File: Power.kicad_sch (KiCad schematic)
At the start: 17 parts, among them Q1 SI2301BDS, U1 ICL7660S, X1 PEDAL_COMBO_TOP

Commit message: Initial layout
Finished the initial PCB layout.
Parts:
- removed X1: PEDAL_COMBO_TOP, Custom_Parts:PEDAL_COMBO_TOP, symbol Custom_Parts:PEDAL_COMBO_TOP
- D2: footprint Diode_SMD:D_SOD-123 -> Diode_SMD:D_SOD-323
- renumbered C4 to C3, C3 to C4, C7 to C6, C6 to C7
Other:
- moved on the sheet: C3, C5, C6, D1, D2, FB1, Q1, R2

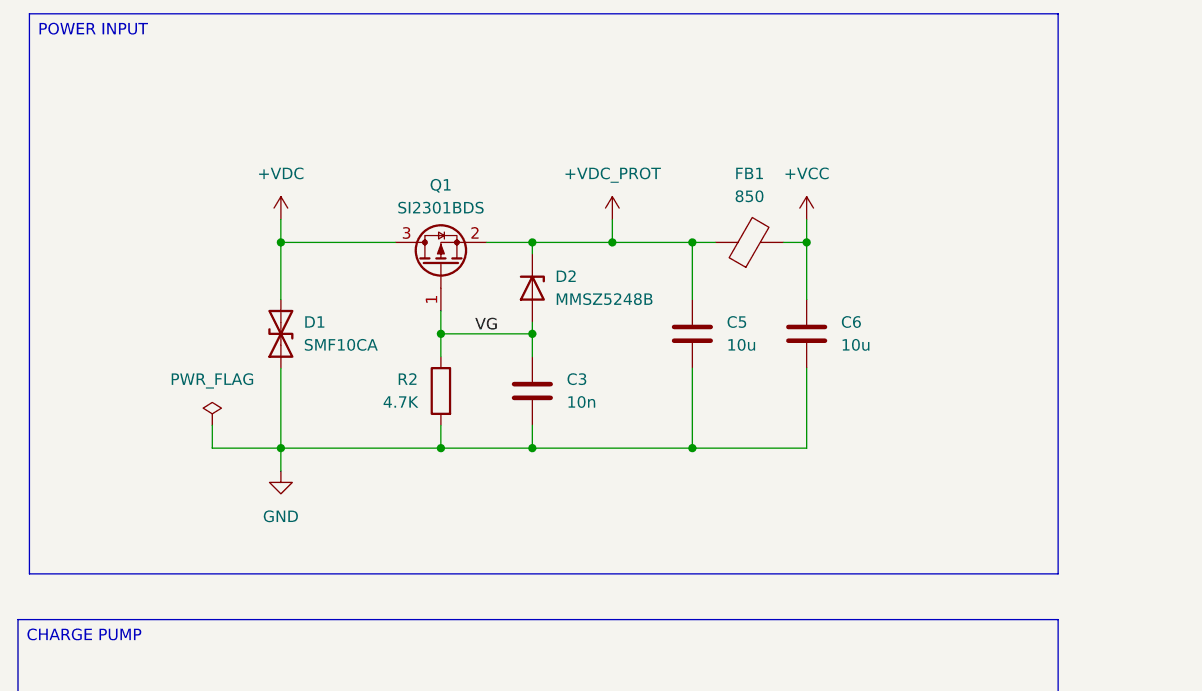
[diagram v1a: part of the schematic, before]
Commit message: Filtering section and layout
Updated the PCB layout.
Added additional input voltage filtering.
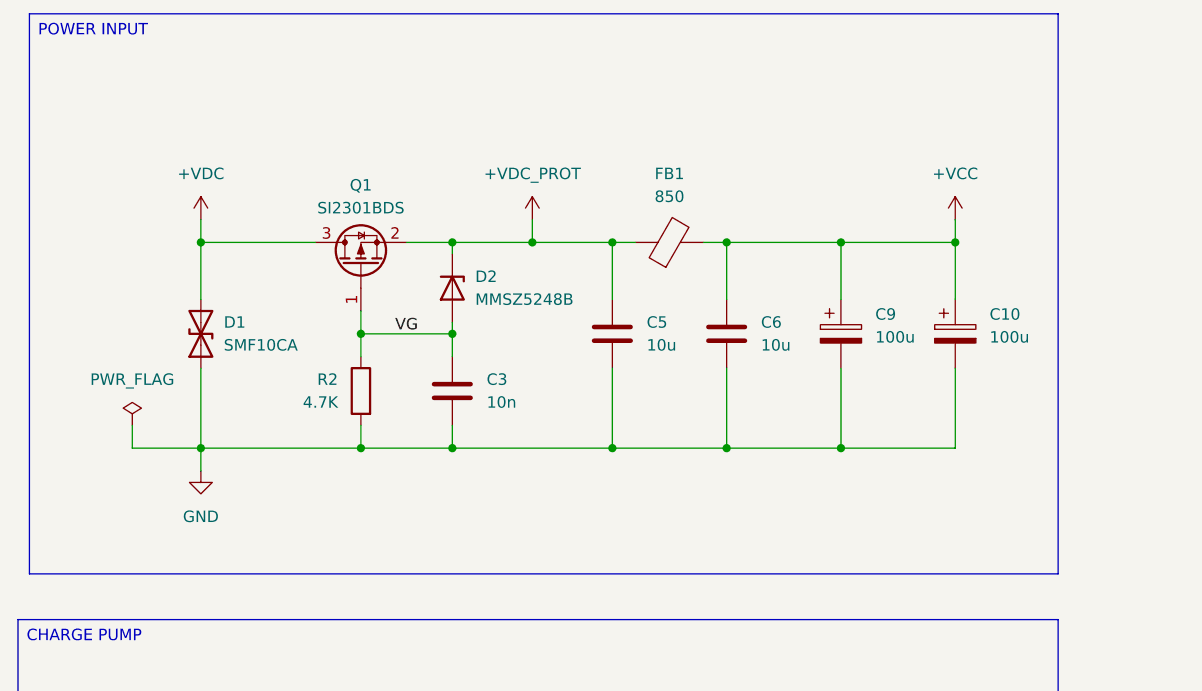
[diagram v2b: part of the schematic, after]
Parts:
- added C10, C9: 100u, Capacitor_SMD:CP_Elec_6.3x5.8, symbol Device:C_Polarized
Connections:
- net +VCC: now also C10.1, C9.1
- net GND: now also C10.2, C9.2
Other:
- moved on the sheet: C3, C5, C6, D1, D2, FB1, Q1, R2

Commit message: Control layout
Updated the layout for the controls.
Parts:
- renumbered C9 to C8, C8 to C9
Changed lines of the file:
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@@
 		(dnp no)
 		(fields_autoplaced yes)
-		(property "Reference" "C8"
+		(property "Reference" "C9"
 			(at 194.31 126.9999 0)
 			(show_name no)
@@
 			(project "EffectsBase"
 				(path "/a2cd04b3-686a-4ef4-b876-d75449c48611/665024c4-4a51-499f-9e43-0b670d7e2fa3"
-					(reference "C8")
+					(reference "C9")
 					(unit 1)
 				)
@@
 		(dnp no)
 		(fields_autoplaced yes)
-		(property "Reference" "#PWR08"
+		(property "Reference" "#PWR07"
 			(at 190.5 119.38 0)
 			(hide yes)
@@
 			(project "EffectsBase"
 				(path "/a2cd04b3-686a-4ef4-b876-d75449c48611/665024c4-4a51-499f-9e43-0b670d7e2fa3"
-					(reference "#PWR08")
+					(reference "#PWR07")
 					(unit 1)
 				)
@@
 		(dnp no)
 		(fields_autoplaced yes)
-		(property "Reference" "#PWR04"
+		(property "Reference" "#PWR03"
 			(at 107.95 81.28 0)
 			(hide yes)
@@
 			(project "EffectsBase"
 				(path "/a2cd04b3-686a-4ef4-b876-d75449c48611/665024c4-4a51-499f-9e43-0b670d7e2fa3"
-					(reference "#PWR04")
+					(reference "#PWR03")
 					(unit 1)
 				)
@@
 		(in_pos_files yes)
 		(dnp no)
-		(property "Reference" "#PWR07"
+		(property "Reference" "#PWR08"
 			(at 191.77 50.8 0)
 			(hide yes)
@@
 			(project "EffectsBase"
 				(path "/a2cd04b3-686a-4ef4-b876-d75449c48611/665024c4-4a51-499f-9e43-0b670d7e2fa3"
-					(reference "#PWR07")
+					(reference "#PWR08")
 					(unit 1)
 				)
@@
 		(dnp no)
 		(fields_autoplaced yes)
-		(property "Reference" "C9"
+		(property "Reference" "C8"
 			(at 182.88 57.5309 0)
 			(show_name no)
@@
 			(project "EffectsBase"
 				(path "/a2cd04b3-686a-4ef4-b876-d75449c48611/665024c4-4a51-499f-9e43-0b670d7e2fa3"
-					(reference "C9")
+					(reference "C8")
 					(unit 1)
 				)
@@
 		(in_pos_files yes)
 		(dnp no)
-		(property "Reference" "#PWR02"
+		(property "Reference" "#PWR04"
 			(at 111.76 119.38 0)
 			(hide yes)
@@
 			(project "EffectsBase"
 				(path "/a2cd04b3-686a-4ef4-b876-d75449c48611/665024c4-4a51-499f-9e43-0b670d7e2fa3"
-					(reference "#PWR02")
+					(reference "#PWR04")
 					(unit 1)
 				)
@@
 		(in_pos_files yes)
 		(dnp no)
-		(property "Reference" "#PWR03"
+		(property "Reference" "#PWR02"
 			(at 107.95 50.8 0)
 			(hide yes)
@@
 			(project "EffectsBase"
 				(path "/a2cd04b3-686a-4ef4-b876-d75449c48611/665024c4-4a51-499f-9e43-0b670d7e2fa3"
-					(reference "#PWR03")
-					(unit 1)
-				)
+					(reference "#PWR02")
+					(unit 1)
+				)

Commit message: Finished layout
Initial PCB layout iteration.
Updated the readme file.
Added board images.
Added output files.
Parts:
- C1, C2, C4, C5, C6, C7, C9: JLCPCB Part (none) -> C15850; Manufacturer Part (none) -> CL21A106KAYNNNE
- C10, C8: JLCPCB Part (none) -> C5246539; Manufacturer Part (none) -> HV1E107M0605PZ; now not fitted; now left out of the parts list
- C3: JLCPCB Part (none) -> C57112; Manufacturer Part (none) -> 0603B103K500NT
- D1: JLCPCB Part (none) -> C19077505; Manufacturer Part (none) -> SMF10CA
- D2: JLCPCB Part (none) -> C22395566; Manufacturer Part (none) -> MMSZ5248BS
- D3: JLCPCB Part (none) -> C8598; Manufacturer Part (none) -> B5819W SL
- FB1: JLCPCB Part (none) -> C13415; Manufacturer Part (none) -> SDCL1608C68NJTDF
- Q1: JLCPCB Part (none) -> C10487; Manufacturer Part (none) -> SI2301CDS-T1-GE3
- R1: JLCPCB Part (none) -> C22775; Manufacturer Part (none) -> 0603WAF1000T5E
- R2: JLCPCB Part (none) -> C23162; Manufacturer Part (none) -> 0603WAF4701T5E
- U1: JLCPCB Part (none) -> C7535; Manufacturer Part (none) -> ICL7660SIBAZT
